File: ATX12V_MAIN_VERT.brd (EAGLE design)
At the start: 27.9 x 58.4 mm, 7 parts, among them J1 ATX12V_MAIN_VERT, J2 1X12, J3 1X12, J4 1X04, J5 1X04, J6 1X04, J7 1X04

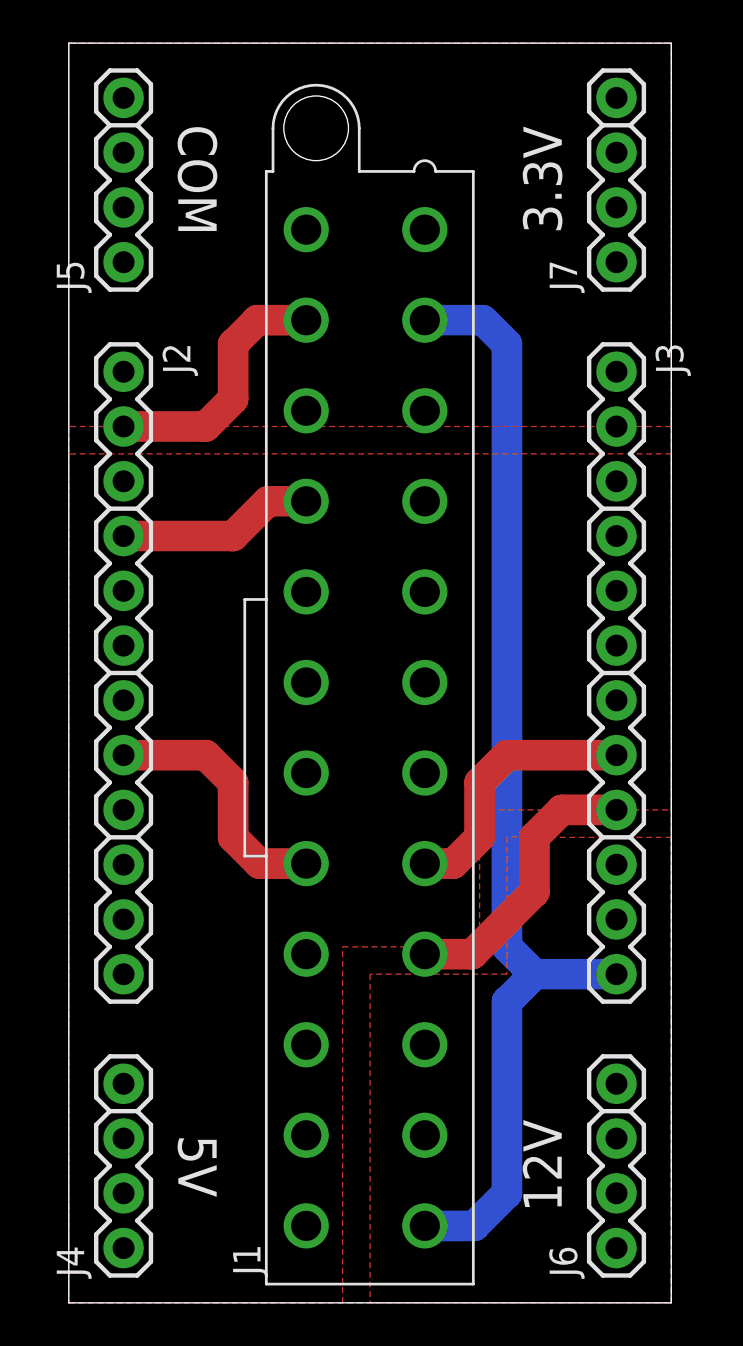
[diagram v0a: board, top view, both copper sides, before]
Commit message: Fix some silk screen flaws in pin header devices.
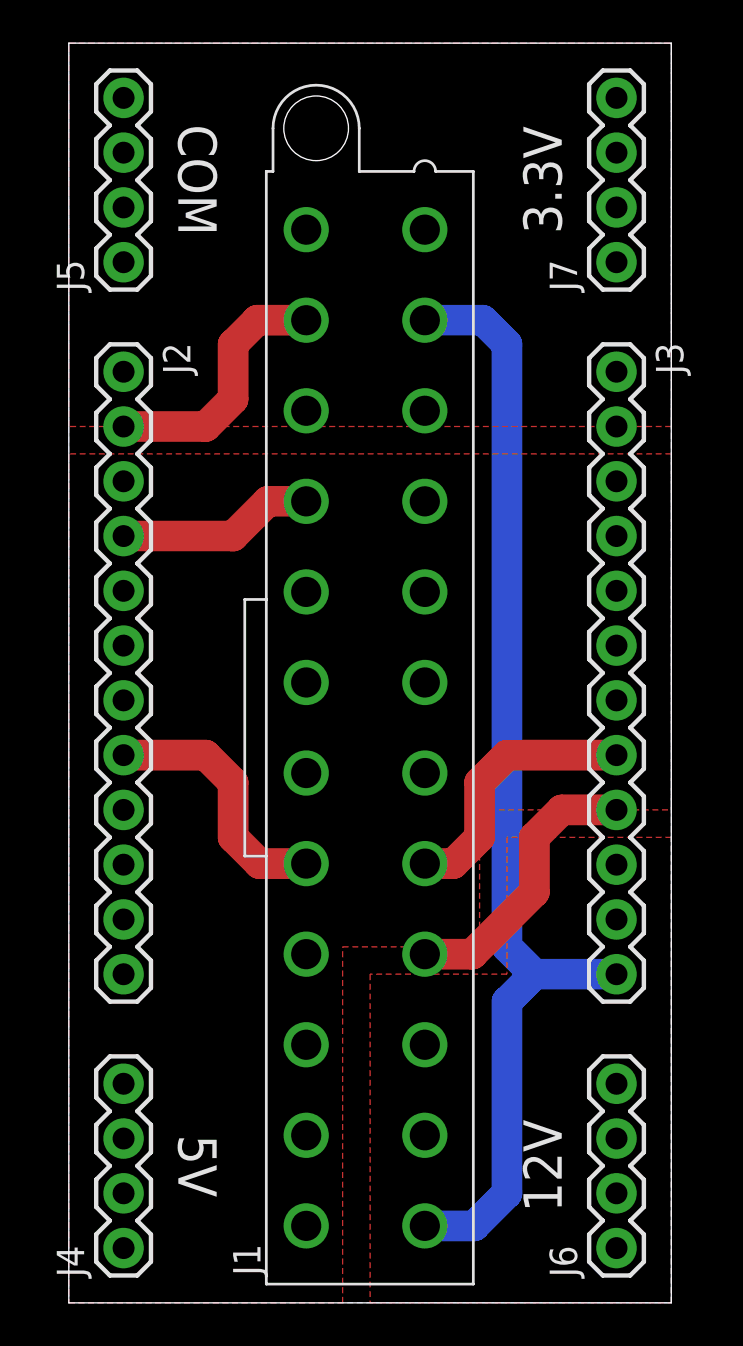
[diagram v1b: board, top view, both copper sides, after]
